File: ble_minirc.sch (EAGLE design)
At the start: 28 parts, among them CN1 B2B-PH-K-S, Q3 MOSFET-NCHANNELSMD, U1 DRV8835, U2 WT51822-S4, U3 MIC5205-3.3YM5-TR

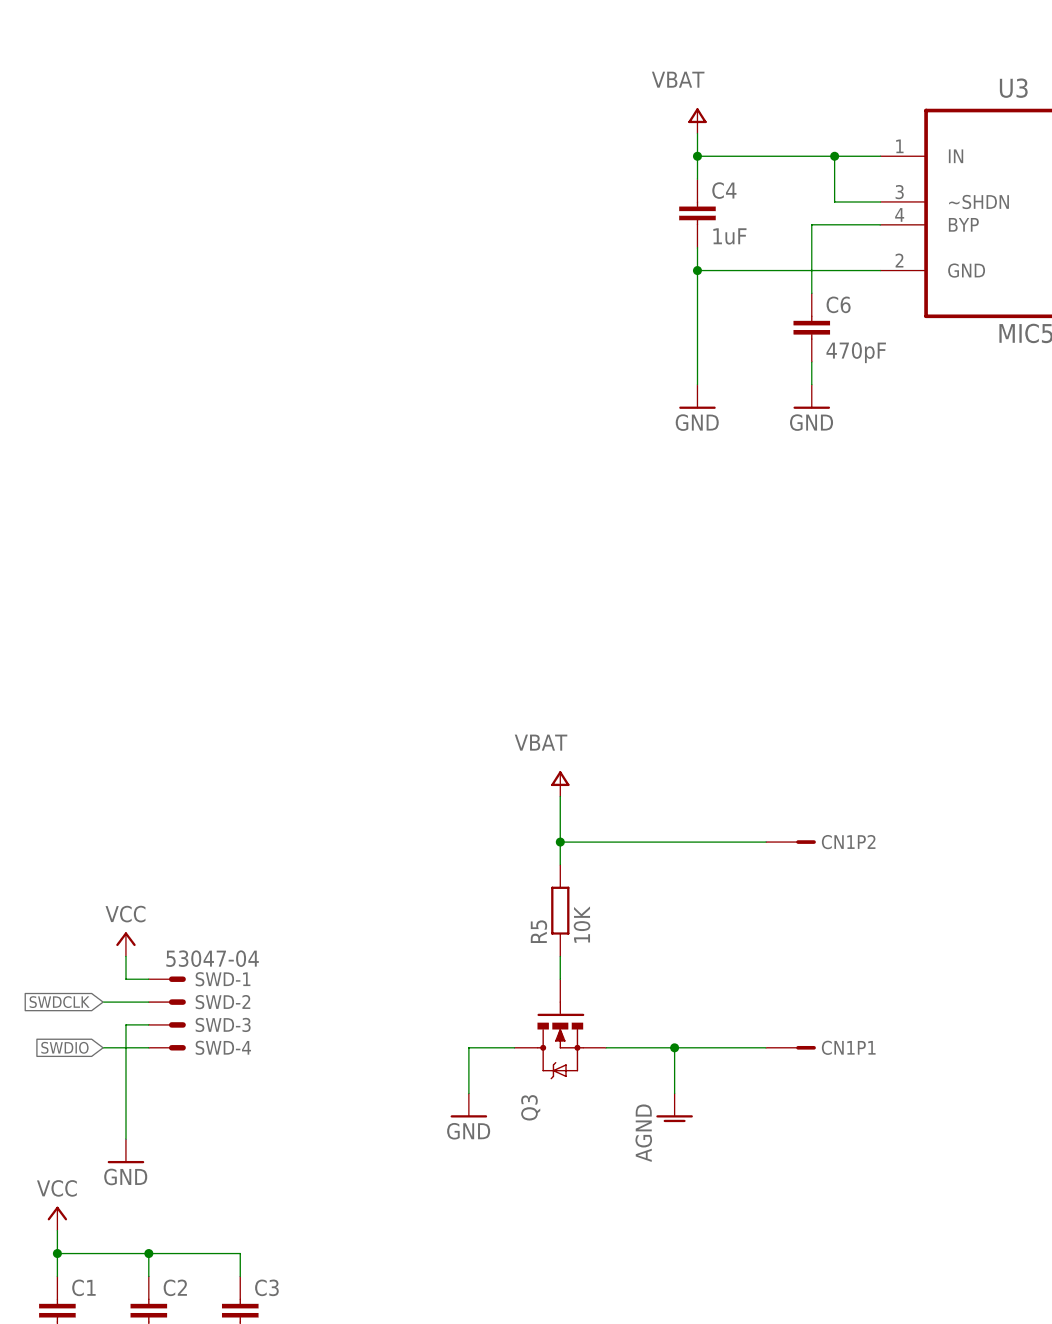
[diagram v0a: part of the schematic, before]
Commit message: Fixed FET direction
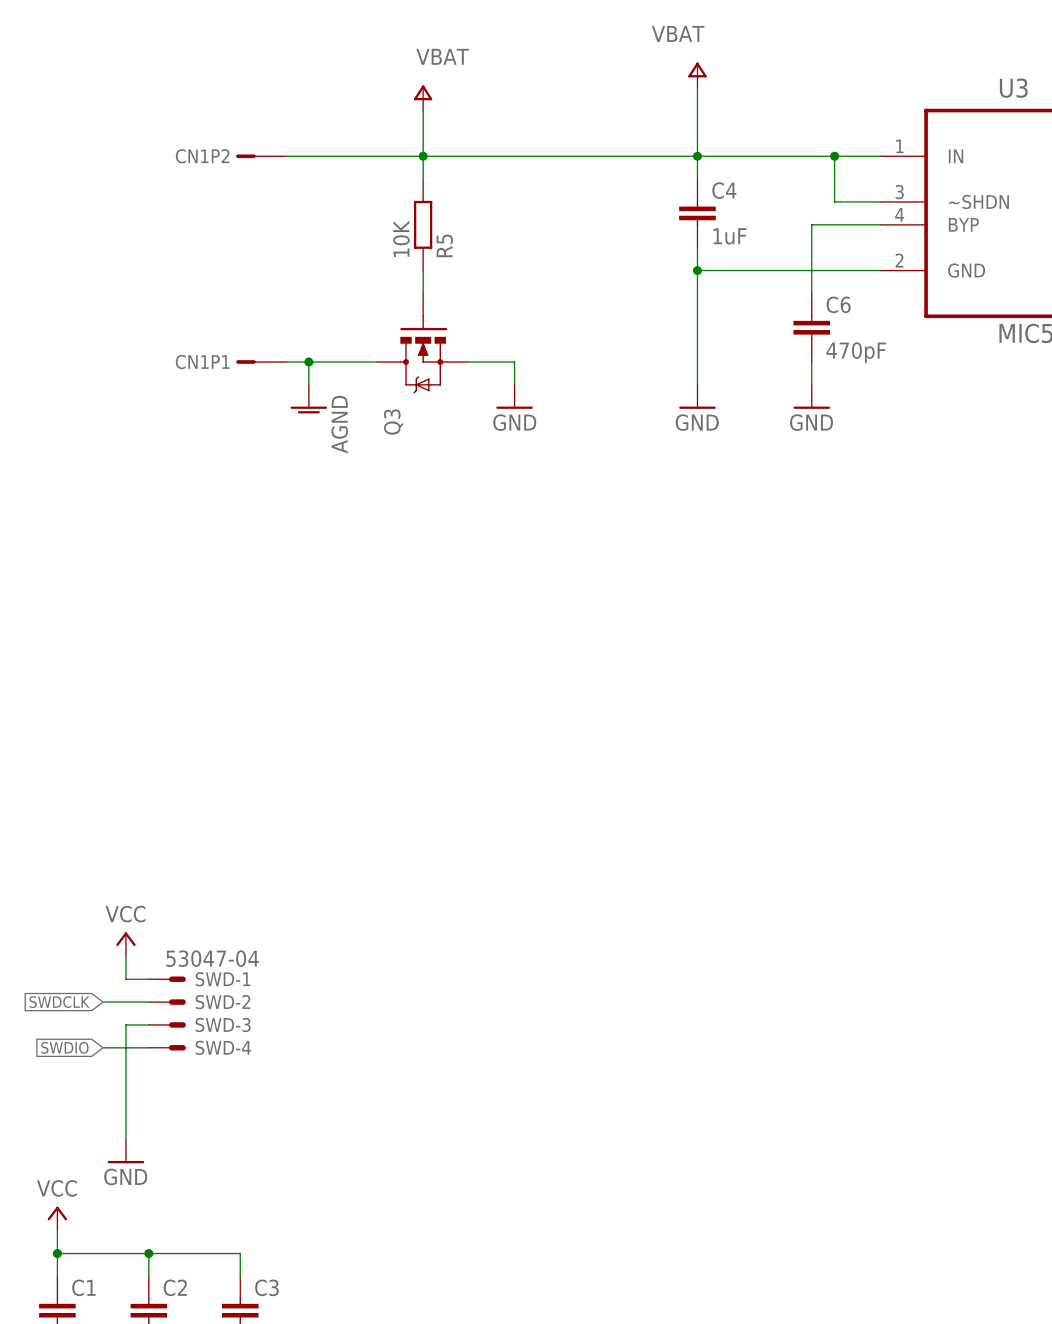
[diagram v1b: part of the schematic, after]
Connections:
- net AGND: now also Q3.D; no longer Q3.S
- net GND: now also Q3.S; no longer Q3.D
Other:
- moved on the sheet: CN1P1, CN1P2, Q3, R5
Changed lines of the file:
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@@
 <?xml version="1.0" encoding="utf-8"?>
 <!DOCTYPE eagle SYSTEM "eagle.dtd">
-<eagle version="8.4.1">
+<eagle version="8.7.0">
 <drawing>
 <settings>
@@
 </instance>
 <instance part="VCC1" gate="G$1" x="109.22" y="198.12"/>
-<instance part="Q3" gate="G$1" x="205.74" y="165.1" rot="MR270"/>
-<instance part="GND1" gate="1" x="195.58" y="157.48"/>
-<instance part="AGND1" gate="VR1" x="218.44" y="157.48"/>
+<instance part="Q3" gate="G$1" x="190.5" y="241.3" rot="MR270"/>
+<instance part="GND1" gate="1" x="200.66" y="236.22" rot="MR0"/>
+<instance part="AGND1" gate="VR1" x="177.8" y="236.22" rot="MR0"/>
 <instance part="GND2" gate="1" x="106.68" y="137.16"/>
 <instance part="GND3" gate="1" x="157.48" y="152.4"/>
 <instance part="VCC4" gate="G$1" x="157.48" y="177.8"/>
-<instance part="R5" gate="G$1" x="205.74" y="180.34" rot="R90"/>
+<instance part="R5" gate="G$1" x="190.5" y="256.54" rot="MR90"/>
 <instance part="C1" gate="G$1" x="149.86" y="137.16"/>
 <instance part="C2" gate="G$1" x="160.02" y="137.16"/>
@@
 <instance part="C6" gate="G$1" x="233.68" y="246.38"/>
 <instance part="GND10" gate="1" x="233.68" y="236.22"/>
-<instance part="U$2" gate="G$1" x="205.74" y="193.04"/>
-<instance part="U$3" gate="G$1" x="220.98" y="266.7"/>
+<instance part="U$2" gate="G$1" x="190.5" y="269.24" rot="MR0"/>
+<instance part="U$3" gate="G$1" x="220.98" y="271.78"/>
 <instance part="TP7" gate="G$1" x="429.26" y="76.2" rot="R270"/>
 <instance part="TP8" gate="G$1" x="429.26" y="63.5" rot="R270"/>
@@
 <instance part="U$1" gate="G$1" x="276.86" y="195.58"/>
 <instance part="GND7" gate="1" x="276.86" y="157.48"/>
-<instance part="CN1" gate="P1" x="233.68" y="165.1"/>
-<instance part="CN1" gate="P2" x="233.68" y="187.96"/>
+<instance part="CN1" gate="P1" x="170.18" y="241.3" rot="MR0"/>
+<instance part="CN1" gate="P2" x="170.18" y="264.16" rot="MR0"/>
 </instances>
 <busses>
@@
 <net name="GND" class="0">
 <segment>
-<pinref part="Q3" gate="G$1" pin="D"/>
 <pinref part="GND1" gate="1" pin="GND"/>
-<wire x1="200.66" y1="165.1" x2="195.58" y2="165.1" width="0.1524" layer="91"/>
-<wire x1="195.58" y1="165.1" x2="195.58" y2="160.02" width="0.1524" layer="91"/>
+<wire x1="200.66" y1="241.3" x2="200.66" y2="238.76" width="0.1524" layer="91"/>
+<pinref part="Q3" gate="G$1" pin="S"/>
+<wire x1="195.58" y1="241.3" x2="200.66" y2="241.3" width="0.1524" layer="91"/>
 </segment>
 <segment>
@@
 <net name="AGND" class="0">
 <segment>
-<pinref part="Q3" gate="G$1" pin="S"/>
-<wire x1="210.82" y1="165.1" x2="218.44" y2="165.1" width="0.1524" layer="91"/>
-<wire x1="218.44" y1="165.1" x2="228.6" y2="165.1" width="0.1524" layer="91"/>
+<wire x1="177.8" y1="241.3" x2="175.26" y2="241.3" width="0.1524" layer="91"/>
 <pinref part="AGND1" gate="VR1" pin="AGND"/>
-<wire x1="218.44" y1="160.02" x2="218.44" y2="165.1" width="0.1524" layer="91"/>
-<junction x="218.44" y="165.1"/>
+<wire x1="177.8" y1="238.76" x2="177.8" y2="241.3" width="0.1524" layer="91"/>
 <pinref part="CN1" gate="P1" pin="1"/>
+<pinref part="Q3" gate="G$1" pin="D"/>
+<wire x1="185.42" y1="241.3" x2="177.8" y2="241.3" width="0.1524" layer="91"/>
+<junction x="177.8" y="241.3"/>
 </segment>
 </net>
@@
 <pinref part="Q3" gate="G$1" pin="G"/>
 <pinref part="R5" gate="G$1" pin="1"/>
-<wire x1="205.74" y1="172.72" x2="205.74" y2="175.26" width="0.1524" layer="91"/>
+<wire x1="190.5" y1="248.92" x2="190.5" y2="251.46" width="0.1524" layer="91"/>
 </segment>
 </net>
@@
 <net name="VBAT" class="0">
 <segment>
-<wire x1="228.6" y1="187.96" x2="205.74" y2="187.96" width="0.1524" layer="91"/>
-<pinref part="R5" gate="G$1" pin="2"/>
-<wire x1="205.74" y1="187.96" x2="205.74" y2="193.04" width="0.1524" layer="91"/>
-<wire x1="205.74" y1="187.96" x2="205.74" y2="185.42" width="0.1524" layer="91"/>
-<junction x="205.74" y="187.96"/>
-<pinref part="U$2" gate="G$1" pin="VBAT"/>
-<pinref part="CN1" gate="P2" pin="1"/>
-</segment>
-<segment>
 <pinref part="U3" gate="A" pin="IN"/>
 <wire x1="241.3" y1="264.16" x2="236.22" y2="264.16" width="0.1524" layer="91"/>
 <wire x1="236.22" y1="264.16" x2="220.98" y2="264.16" width="0.1524" layer="91"/>
-<wire x1="220.98" y1="264.16" x2="220.98" y2="266.7" width="0.1524" layer="91"/>
+<wire x1="220.98" y1="264.16" x2="220.98" y2="271.78" width="0.1524" layer="91"/>
 <pinref part="C4" gate="G$1" pin="1"/>
 <wire x1="220.98" y1="261.62" x2="220.98" y2="264.16" width="0.1524" layer="91"/>
@@
 <junction x="236.22" y="264.16"/>
 <pinref part="U$3" gate="G$1" pin="VBAT"/>
-</segment>
-<segment>
+<wire x1="220.98" y1="264.16" x2="190.5" y2="264.16" width="0.1524" layer="91"/>
+<wire x1="175.26" y1="264.16" x2="190.5" y2="264.16" width="0.1524" layer="91"/>
+<pinref part="R5" gate="G$1" pin="2"/>
+<wire x1="190.5" y1="264.16" x2="190.5" y2="269.24" width="0.1524" layer="91"/>
+<wire x1="190.5" y1="264.16" x2="190.5" y2="261.62" width="0.1524" layer="91"/>
+<junction x="190.5" y="264.16"/>
+<pinref part="U$2" gate="G$1" pin="VBAT"/>
+<pinref part="CN1" gate="P2" pin="1"/>
+</segment>
+<segment>
